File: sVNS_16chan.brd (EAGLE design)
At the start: 38.4 x 25.1 mm, 56 parts, among them IC2 OPA990IDCKR, IC3 EFM8SB10F2G-A-QFN20, J1 M50-3631042, J2 M50-3631042, J3 M50-3631042, U1 NT3H2211W0FHKH, U2 LT8410EDC-1#TRMPBF, U3 MUX36S16IRSNR, U4 MUX36S16IRSNR

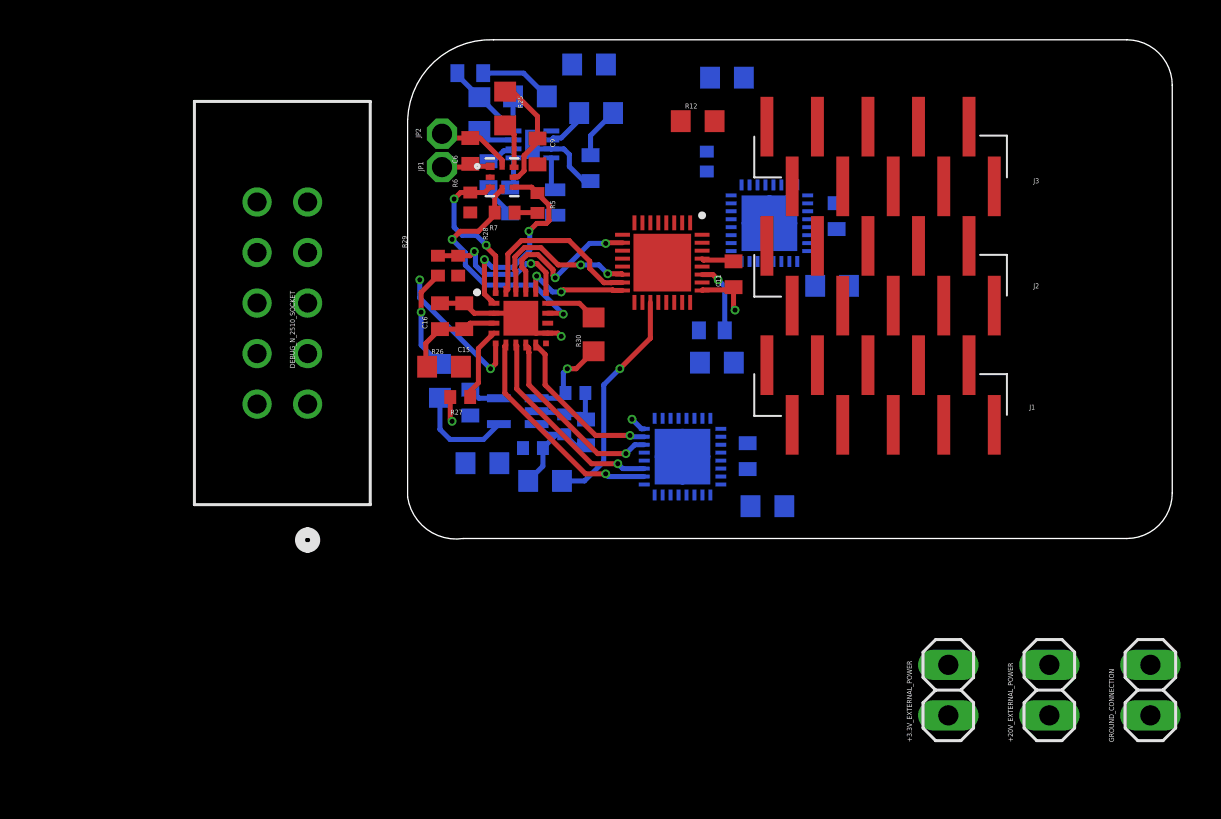
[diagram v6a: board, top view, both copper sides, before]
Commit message: Checkpoint 3. Output stage pin nets to be removed.
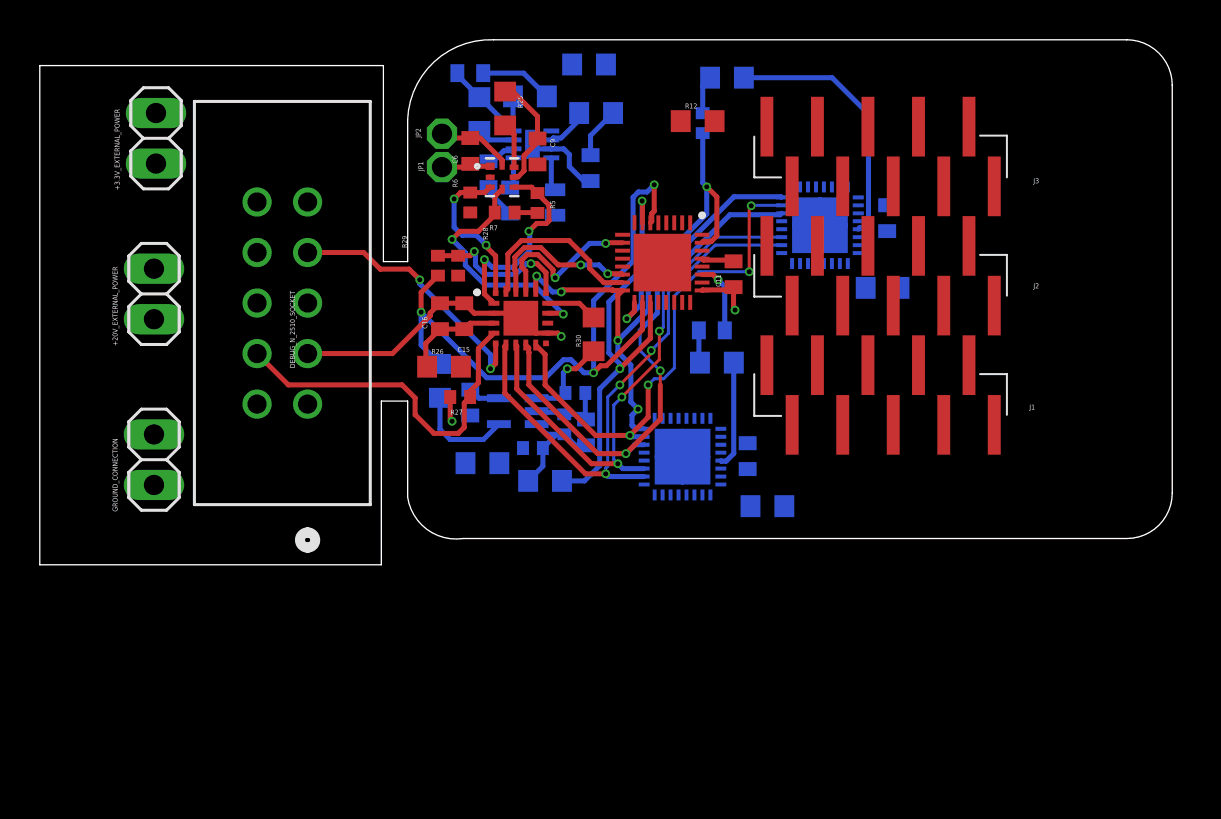
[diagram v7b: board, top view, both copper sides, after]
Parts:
- moved GROUND_CONNECTION 51.4 mm to (-13.3, 3.96)
- moved +20V_EXTERNAL_POWER 49.2 mm to (-13.3, 12.3)
- moved +3.3V_EXTERNAL_POWER 48.5 mm to (-13.2, 20.1)
- moved C5 2.54 mm to (23.6, 16.1)
- moved R20 2.54 mm to (23.4, 12.6)
- moved U4 2.54 mm to (20.2, 15.7)
- moved R13 1.94 mm to (14.3, 20.9)
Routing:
- net I_OUT+: track 5.18 -> 33.5 mm, vias 1 -> 3
- net P0.5_SHDN: track 6.30 -> 25.7 mm, vias 3 -> 4
- net P1.5_MUXS16_A1: track 9.48 -> 27.1 mm, vias 1 -> 2
- net P1.3_MUXS16_A0: track 8.26 -> 25.6 mm, vias 1 -> 4
- net P1.7_MUXS16_A3: track 11.2 -> 28.3 mm, vias 1 -> 3
- net P1.6_MUXS16_A2: track 10.3 -> 27.2 mm, vias 1 -> 3
- net DB: track 0.00 -> 15.6 mm, vias 0 -> 2
- net RSTB_/_C2CK: track 3.72 -> 18.1 mm
- net BAL_B: track 0.00 -> 13.2 mm
- net I_OUT-: track 11.5 -> 21.9 mm, vias 1 -> 2
- net GND: track 23.8 -> 31.6 mm
- net P2.7_/_C2D: track 7.33 -> 13.5 mm
- net BAL_A: track 0.00 -> 5.39 mm
- net BAL_B_PIN: track 0.00 -> 1.94 mm
- net BAL_A_PIN: track 0.00 -> 1.65 mm
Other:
- board size 38.4 x 25.1 mm -> 56.9 x 26.4 mm

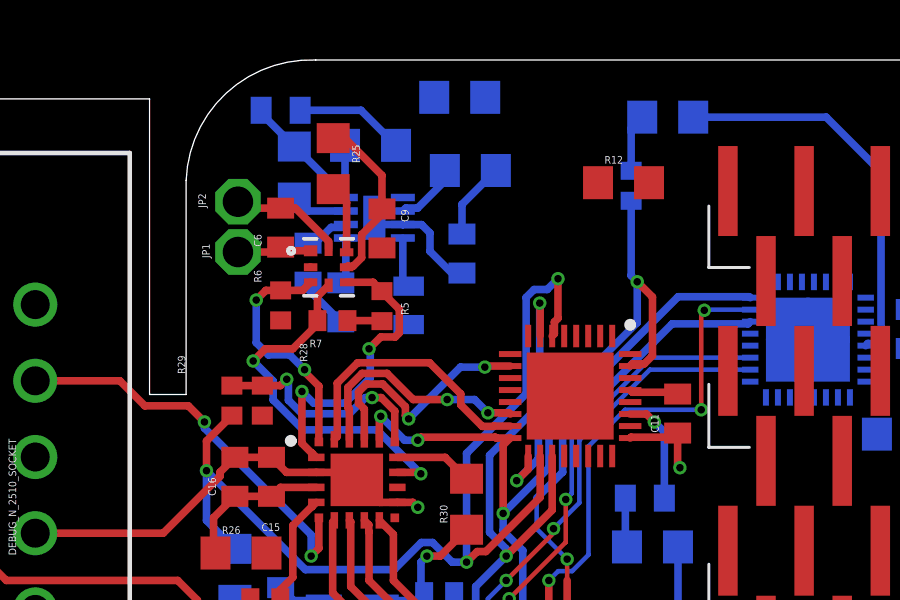
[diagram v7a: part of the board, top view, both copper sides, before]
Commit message: Checkpoint 4. Output stage pin nets removed.
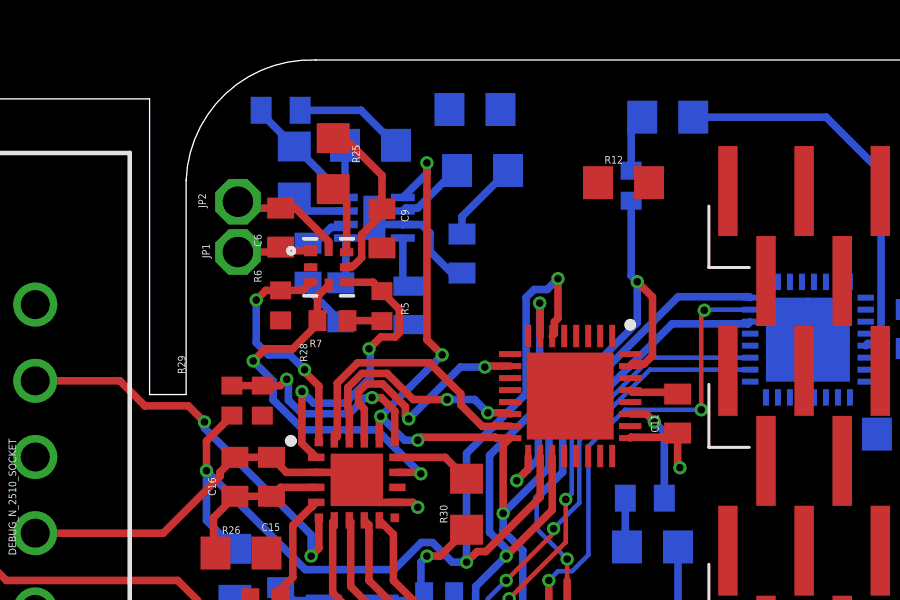
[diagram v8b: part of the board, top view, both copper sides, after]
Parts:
- moved R24 0.65 mm to (9.12, 23.4)
- moved R23 0.41 mm to (9.37, 21.4)
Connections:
- net S10A: no longer J1.10
- net S10B: no longer J3.10
- net S11A: no longer J2.1
- net S11B: no longer J2.5
- net S12A: no longer J2.2
- net S12B: no longer J2.6
- net S13A: no longer J2.3
- net S13B: no longer J2.7
- net S14A: no longer J2.4
- net S14B: no longer J2.8
- net S1A: no longer J1.1
- net S1B: no longer J3.1
- net S2A: no longer J1.2
- net S2B: no longer J3.2
- net S3A: no longer J1.3
- net S3B: no longer J3.3
- net S4A: no longer J1.4
- net S4B: no longer J3.4
- net S5A: no longer J1.5
- net S5B: no longer J3.5
- net S6A: no longer J1.6
- net S6B: no longer J3.6
- net S7A: no longer J1.7
- net S7B: no longer J3.7
- net S8A: no longer J1.8
- net S8B: no longer J3.8
- net S9A: no longer J1.9
- net S9B: no longer J3.9
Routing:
- net P0.5_SHDN: track 25.7 -> 36.6 mm, vias 4 -> 6
